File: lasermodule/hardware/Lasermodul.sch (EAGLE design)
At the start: 88 parts, among them IC1 MEGA8-AI

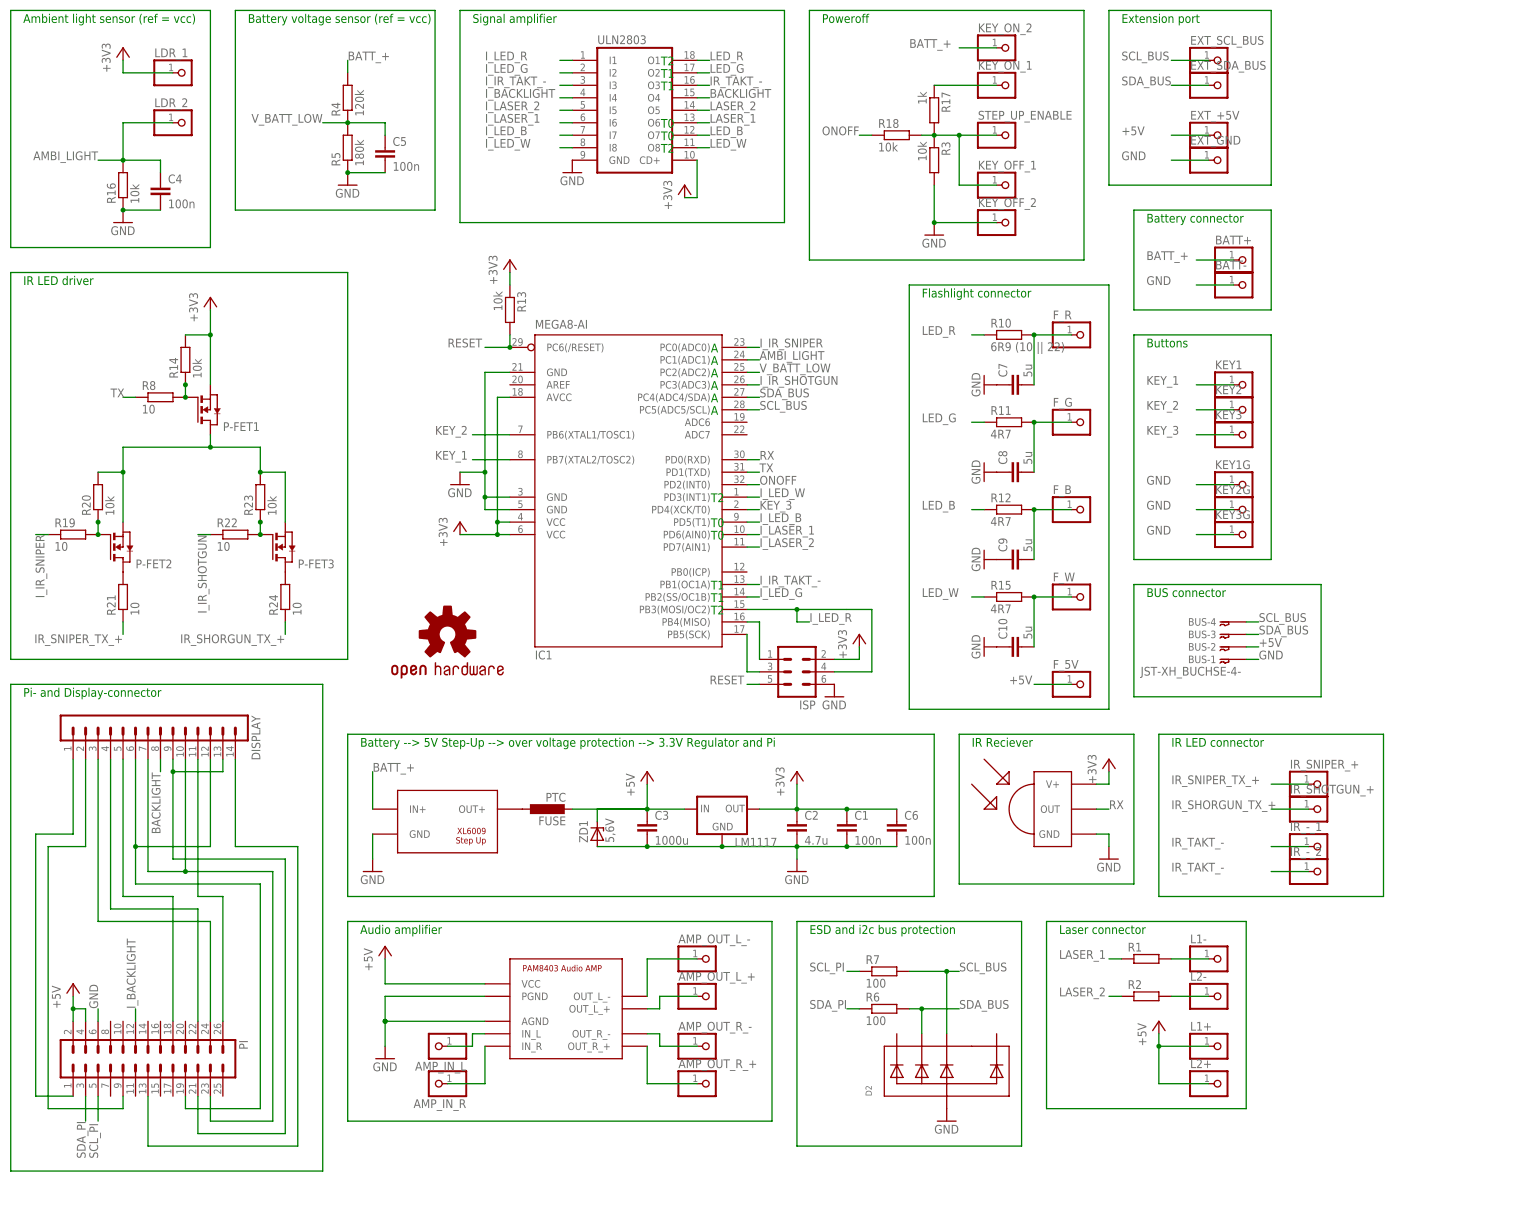
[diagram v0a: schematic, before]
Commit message: lasermodul: reverse polarity protection
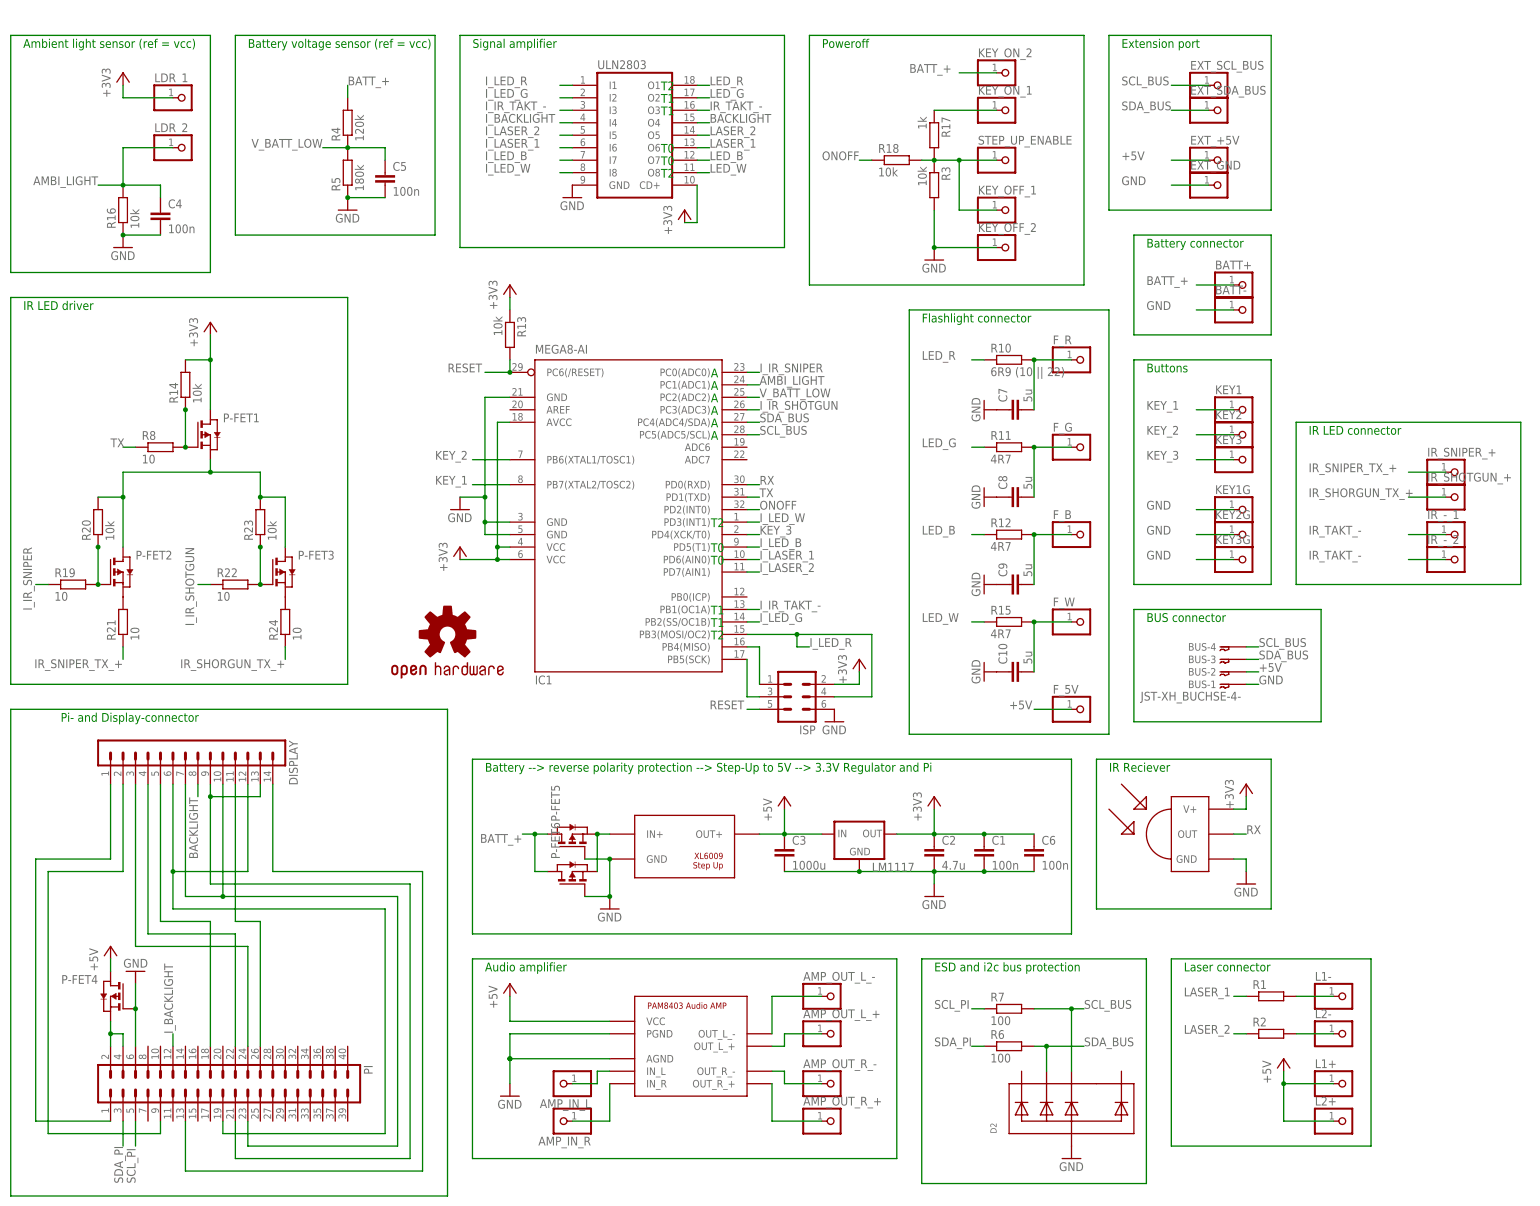
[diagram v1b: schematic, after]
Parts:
- removed FUSE: PTC, resistor:L-EUL1812
- removed ZD1: 5,6V, wz:Z-DIODE
- added P-FET4, P-FET5, P-FET6: (no value), zetex:PMOSSOT23
- P-FET1, P-FET2, P-FET3: device zetex:NMOSSOT23 -> zetex:PMOSSOT23
- PI: device con-lstb:MA13-2 -> con-lstb:MA20-2
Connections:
- removed net N$28: FUSE.1, U$3.OUT+
- new net N$46: P-FET4.S, PI.2, PI.4
- new net N$54: P-FET5.S, P-FET6.S, U$3.IN+
- net +3V2: now also P-FET1.S, P-FET2.D, P-FET3.D; no longer P-FET1.D, P-FET2.S, P-FET3.S
- net +3V3: now also P-FET1.D; no longer P-FET1.S
- net +5V: now also P-FET4.D, U$3.OUT+; no longer FUSE.2, PI.2, PI.4, ZD1.C
- net BATT_+: now also P-FET5.D, P-FET6.D; no longer U$3.IN+
- net GND: now also P-FET4.G, P-FET5.G, P-FET6.G; no longer ZD1.A
- net N$34: now also P-FET2.S; no longer P-FET2.D
- net N$53: now also P-FET3.S; no longer P-FET3.D
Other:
- note added: "Battery --> reverse polarity protection --> Step-Up to 5V --> 3.3V Regulator and Pi"
- note removed: "Battery --> 5V Step-Up --> over voltage protection --> 3.3V Regulator and Pi"
- moved on the sheet: AMP_IN_L, AMP_IN_R, AMP_OUT_L_+, AMP_OUT_L_-, AMP_OUT_R_+, AMP_OUT_R_-, BATT+, BATT-, BUS-1, BUS-2, BUS-3, BUS-4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

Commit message: another onoff
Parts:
- removed KEY_OFF_1, KEY_OFF_2, KEY_ON_1, KEY_ON_2, STEP_UP_ENABLE: (no value), wz:PIN-HEADER-1
- removed P-FET5, P-FET6: (no value), zetex:PMOSSOT23
- removed R17: 1k, wz:R_EU0603
- removed R18, R3: 10k, wz:R_EU0603
- added OFF_1, OFF_2, ON_1, ON_2: (no value), wz:PIN-HEADER-1
- added OK1: SFH6186-2, optocoupler:SFH6186-2
- added ON, REV: (no value), wz:N-MOSFET
- added R25: 270, wz:R_EU0603
- added R9: 10k, wz:R_EU0603
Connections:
- net IR_SHORGUN_TX_+ renamed IR_SHOTGUN_TX_+
- removed net N$26: KEY_ON_1.1, R17.1
- removed net N$54: P-FET5.S, P-FET6.S, U$3.IN+
- removed net STEPUP_EN: KEY_OFF_1.1, R17.2, R18.2, R3.1, STEP_UP_ENABLE.1
- new net BATT_-: REV.D
- new net N$28: ON.S, R9.1, REV.S
- new net ONOFF_2: OK1.EMIT, ON.G, ON_2.1, R9.2
- net +3V3: now also R25.2
- net BATT_+: now also OK1.COL, ON_1.1, REV.G, U$3.IN+; no longer KEY_ON_2.1, P-FET5.D, P-FET6.D
- net GND: now also OFF_1.1, OK1.C, ON.D; no longer KEY_OFF_2.1, P-FET5.G, P-FET6.G, R3.2
- net ONOFF: now also IC1.PB0(ICP), OFF_2.1, OK1.A, R25.1; no longer R18.1
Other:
- note added: "Battery --> reverse polarity protection --> on/off --> Step-Up to 5V --> 3.3V Regulator and Pi"
- note removed: "Battery --> reverse polarity protection --> Step-Up to 5V --> 3.3V Regulator and Pi"
- note removed: "Poweroff"
- moved on the sheet: AMP_IN_L, AMP_IN_R, AMP_OUT_L_+, AMP_OUT_L_-, AMP_OUT_R_+, AMP_OUT_R_-, C1, C2, C3, C6, D2, IR_-_1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

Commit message: lasermodul routing started
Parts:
- removed AMP_OUT_L_+, AMP_OUT_L_-, AMP_OUT_R_+, AMP_OUT_R_-, EXT_+5V, EXT_GND, EXT_SCL_BUS, EXT_SDA_BUS, F_5V, F_B, F_G, F_R, F_W, IR_-_1, IR_-_2, IR_SHOTGUN_+, IR_SNIPER_+, L1+, L1-, L2+, L2-: (no value), wz:PIN-HEADER-1
- removed BUS: JST-XH_BUCHSE-4-, wz:JST-XH_BUCHSE-4-
- removed P-FET4: (no value), zetex:PMOSSOT23
- removed R1, R2: (no value), wz:R_EU0603
- added 2A_4A: PTC_FUSE, wz:PTC_FUSE
- added AMP_IN_AGND, AMP_OUT_L+, AMP_OUT_L-, AMP_OUT_R+, AMP_OUT_R-, FLASHL_5V, FLASHL_B, FLASHL_G, FLASHL_R, FLASHL_W, IR_SHOTGUN+, IR_SHOTGUN-, IR_SNIPER+, IR_SNIPER-, LASER_1+, LASER_1-, LASER_2+, LASER_2-: (no value), wz:PIN-HEADER-1PIN-HEADER-1
- added BUS1, EXT_PORT: JST-XH_BUCHSE-4-, wz:JST-XH_BUCHSE-4-
- added C11: 4.7u, wz:C_EU0805
- added C12: 1000u, wz:C_EUCAP_UNIVERSAL
- added C13: 100n, wz:C_EU0603
- added D1(O): DIODEDIODE_SMA_CLOSED, wz:DIODEDIODE_SMA_CLOSED
- added L1(O), L2(O): L, wz:L
- added R1(O), R2(O): (no value), wz:R_EU0603_CLOSED
- added R3(O): (no value), wz:R_EU0805_CLOSED
- AMP_IN_L, AMP_IN_R, KEY1, KEY1G, KEY2, KEY2G, KEY3, KEY3G, LDR_1, LDR_2, OFF_1, OFF_2, ON_1, ON_2: device wz:PIN-HEADER-1 -> wz:PIN-HEADER-1PIN-HEADER-1
- BATT+, BATT-: device wz:PIN-HEADER-1 -> wz:PIN-HEADER-1PIN-HEADER-1_BIG
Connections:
- net +3V2 renamed EASTEREGG_NET
- net I_IR_TAKT_- renamed I_IR_CLK_-
- net I_LED_B renamed I_FLASHL_B
- net I_LED_G renamed I_FLASHL_G
- net I_LED_R renamed I_FLASHL_R
- net I_LED_W renamed I_FLASHL_W
- net LED_B renamed FLASHL_B
- net LED_G renamed FLASHL_G
- net LED_R renamed FLASHL_R
- net LED_W renamed FLASHL_W
- net N$1 renamed LCD_TOUCH_IRQ
- net N$2 renamed LCD_TOUCH_CS
- net N$35 renamed AMP_IN_L
- net N$36 renamed AMP_IN_R
- net N$47 renamed LCD_DC
- net N$48 renamed LCD_MOSI
- net N$49 renamed LCD_MISO
- net N$50 renamed LCD_RESET
- net N$51 renamed LCD_SCK
- net N$52 renamed LCD_CS
- net V_BATT_LOW renamed BATT+_ADC
- removed net BATT_+: BATT+.1, OK1.COL, ON_1.1, R4.2, REV.G, U$3.IN+
- removed net BATT_-: REV.D
- removed net IR_TAKT_-: IR_-_1.1, IR_-_2.1, ULN2803.O3
- removed net N$12: L1-.1, R1.2
- removed net N$37: AMP_OUT_L_+.1, U$4.OUT_L_+
- removed net N$38: AMP_OUT_L_-.1, U$4.OUT_L_-
- removed net N$39: AMP_OUT_R_-.1, U$4.OUT_R_-
- removed net N$40: AMP_OUT_R_+.1, U$4.OUT_R_+
- new net AMP_IN_AGND: AMP_IN_AGND.1, U$4.AGND
- new net AMP_OUT_L+: AMP_OUT_L+.1, U$4.OUT_L_+
- new net AMP_OUT_L-: AMP_OUT_L-.1, U$4.OUT_L_-
- new net AMP_OUT_R+: AMP_OUT_R+.1, U$4.OUT_R_+
- new net AMP_OUT_R-: AMP_OUT_R-.1, U$4.OUT_R_-
- new net BATT+: 2A_4A.1, BATT+.1, R4.2
- new net BATT+_FUSE: 2A_4A.2, OK1.COL, ON_1.1, REV.G, U$3.IN+
- new net BATT-: BATT-.1, REV.D
- new net IR_CLK_-: IR_SHOTGUN-.1, IR_SNIPER-.1, ULN2803.O3
- new net LASER_1-: LASER_1-.1, R1(O).2
- new net LASER_2-: LASER_2-.1, R2(O).2
- new net N$27: L1(O).1, U$3.OUT+
- net +3V3: now also C11.1
- net +5V: now also BUS1-2.1, C12.1, D1(O).A, EXT_PORT-2.1, FLASHL_5V.1, L1(O).2, LASER_1+.1, LASER_2+.1, R3(O).1; no longer BUS-2.1, EXT_+5V.1, F_5V.1, L1+.1, L2+.1, P-FET4.D, U$3.OUT+, U$4.VCC
- net GND: now also BUS1-1.1, C11.2, C12.2, C13.1, DISPLAY.2, EXT_PORT-1.1, PI.14, PI.20, PI.25, PI.30, PI.34, PI.39, PI.9; no longer BATT-.1, BUS-1.1, EXT_GND.1, P-FET4.G, U$4.AGND
- net IR_SHOTGUN_TX_+: now also IR_SHOTGUN+.1; no longer IR_SHOTGUN_+.1
- net IR_SNIPER_TX_+: now also IR_SNIPER+.1; no longer IR_SNIPER_+.1
- net LASER_1: now also R1(O).1; no longer R1.1
- net LASER_2: now also R2(O).1; no longer R2.1
- net N$15: now also FLASHL_R.1; no longer F_R.1
- net N$18: now also C13.2, IC1.AREF; no longer L2-.1, R2.2
- net N$21: now also FLASHL_G.1; no longer F_G.1
- net N$22: now also FLASHL_B.1; no longer F_B.1
- net N$23: now also FLASHL_W.1; no longer F_W.1
- net N$44: now also D1(O).C, PI.2, PI.4; no longer PI.1
- net N$45: now also L2(O).2, R3(O).2; no longer DISPLAY.2, PI.9
- net N$46: now also L2(O).1, U$4.VCC; no longer P-FET4.S, PI.2, PI.4
- net SCL_BUS: now also BUS1-4.1, EXT_PORT-4.1; no longer BUS-4.1, EXT_SCL_BUS.1
- net SDA_BUS: now also BUS1-3.1, EXT_PORT-3.1; no longer BUS-3.1, EXT_SDA_BUS.1
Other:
- note added: "...(O) = optional, with cut bridge"
- note added: "Ambient light sensor (ref = 3.3V)"
- note added: "Atmega --> ULN --> Outputs"
- note added: "Audio"
- note added: "Battery --> self resetting fuse --> reverse polarity protection --> on/off --> Step-Up to 5V --> 3.3V Regulator and Pi"
- note added: "Battery voltage sensor (ref = 3.3V)"
- note added: "Button connector"
- note added: "D"
- note added: "Extension connector"
- note added: "Hitpoint-BUS"
- note added: "IR LED driver and connector"
- note added: "I_... = weak signal between avr io and fet input"
- note added: "Inputs"
- note added: "Lasertag Weapon Raspberry Pi shield warpzone.ms/wiki/projekte:lasertag"
- note added: "Legend"
- note added: "ON-button between ON_1 and ON_2 OFF-button between OFF_1 and OFF_2"
- note added: "S"
- note removed: "Ambient light sensor (ref = vcc)"
- note removed: "Battery --> reverse polarity protection --> on/off --> Step-Up to 5V --> 3.3V Regulator and Pi"
- note removed: "Battery connector"
- note removed: "Battery voltage sensor (ref = vcc)"
- note removed: "Buttons"
- note removed: "Extension port"
- note removed: "IR LED connector"
- note removed: "IR LED driver"
- moved on the sheet: AMP_IN_L, AMP_IN_R, BATT+, BATT-, C1, C10, C2, C3, C4, C5, C6, C7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
